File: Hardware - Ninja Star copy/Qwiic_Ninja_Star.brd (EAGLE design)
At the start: 87.6 x 41.9 mm, 29 parts, among them J1 QWIIC_RIGHT_ANGLE, J2 QWIIC_RIGHT_ANGLE, J3 QWIIC_RIGHT_ANGLE, J4 QWIIC_RIGHT_ANGLE

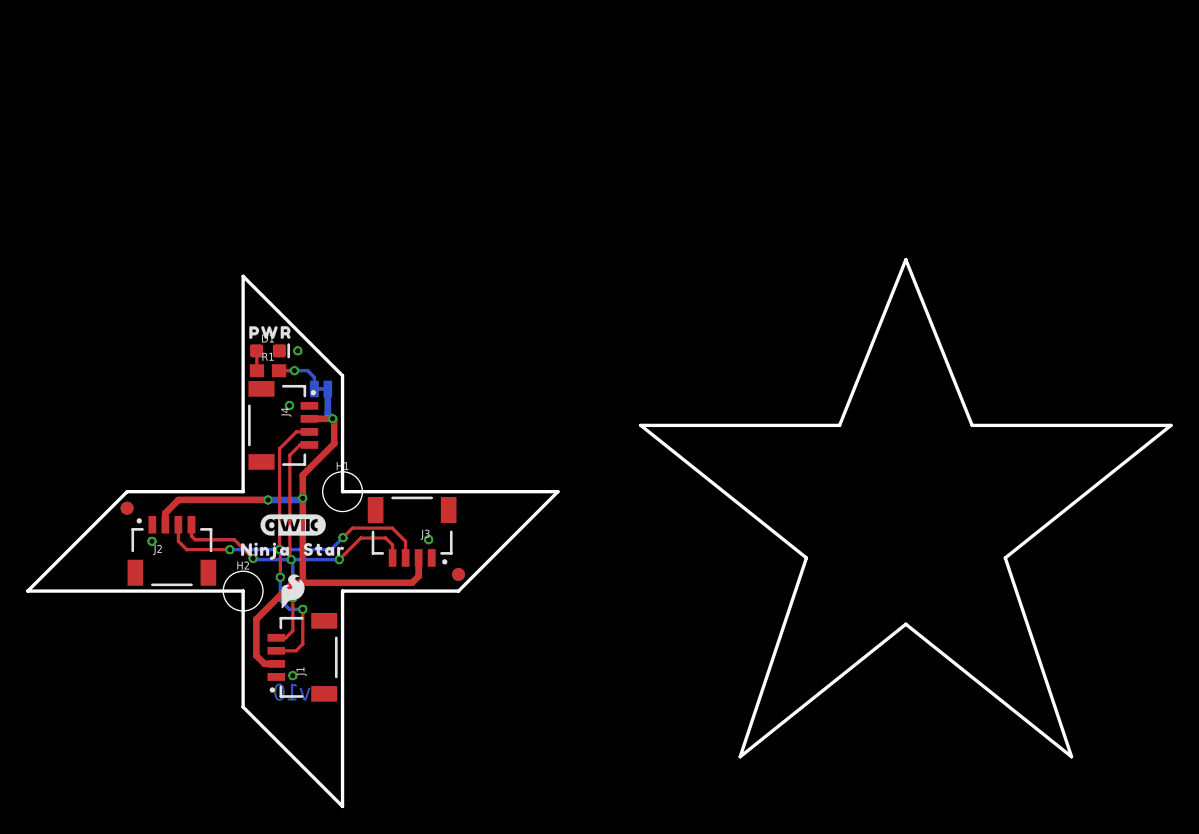
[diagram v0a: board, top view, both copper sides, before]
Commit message: Created star-shaped Qwiic Ninja Star and updated Multi Port
Updated Qwiic Multi Port with QC Double check concerns:
Removed wire stub
Approve DRC errors
Move via to not clip the t in "Port" on top
Moved power jumper and silk so that jumper silk and SF logo don't overlap
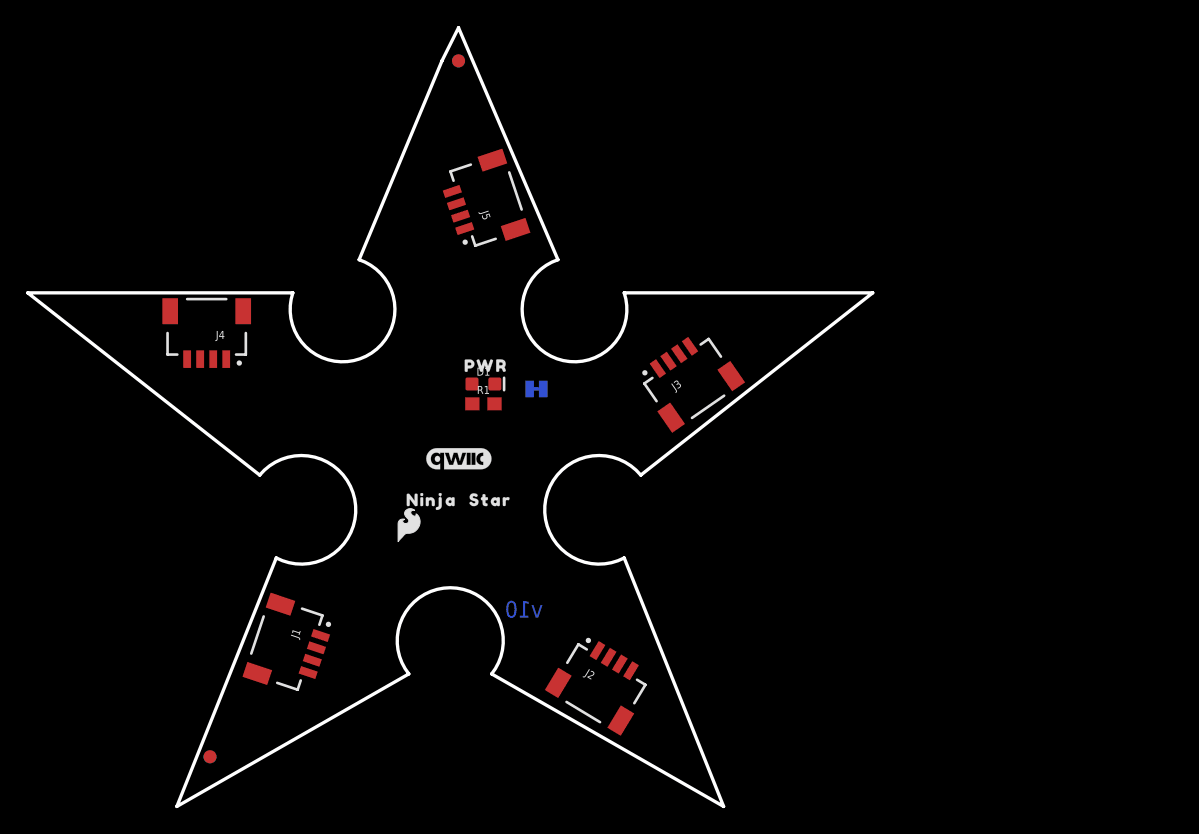
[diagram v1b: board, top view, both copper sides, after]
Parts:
- removed H1, H2: STAND-OFFTIGHT, SparkFun-Hardware:STAND-OFF-TIGHT
- added J5: QWIIC_RIGHT_ANGLE, SparkFun-Connectors:JST04_1MM_RA
- moved FD3 39.4 mm to (33.0, 57.1)
- moved FD4 39.4 mm to (33.0, 57.1)
- moved J2 35.5 mm to (45.0, 11.2), turned to 328.9 degrees
- moved J3 25.3 mm to (49.5, 34.4), turned to 34.7 degrees
- moved LOGO8 24.7 mm to (23.7, 32.1)
- moved LOGO7 21.3 mm to (29.0, 23.6)
- moved FD1 20.1 mm to (14.0, 3.81)
- moved FD2 20.1 mm to (14.0, 3.81)
- moved LOGO1 18.9 mm to (38.1, 20.3)
- moved LOGO3 18.9 mm to (33.0, 39.4)
- moved U$5 18.9 mm to (40.6, 18.5)
- moved U$7 18.9 mm to (40.3, 17.1)
- moved R1 16.7 mm to (34.9, 30.9)
- moved U$9 16.7 mm to (32.8, 33.8)
- moved D1 16.7 mm to (34.9, 32.4)
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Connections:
- net 3.3V: now also J5.2
- net GND: now also J5.1
- net SCL: now also J5.4
- net SDA: now also J5.3
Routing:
- net 3.3V: track 49.6 -> 0.00 mm, vias 3 -> 0
- net SDA: track 42.7 -> 0.00 mm, vias 5 -> 0
- net SCL: track 35.8 -> 0.00 mm, vias 4 -> 0
- net N$2: track 3.81 -> 0.02 mm, vias 1 -> 0
- net N$1: track 1.54 -> 0.00 mm
- removed copper zone on layer 1, net GND
- removed copper zone on layer 16, net GND
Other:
- board size 87.6 x 41.9 mm -> 64.8 x 59.7 mm

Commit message: Wired qwiic ninja star
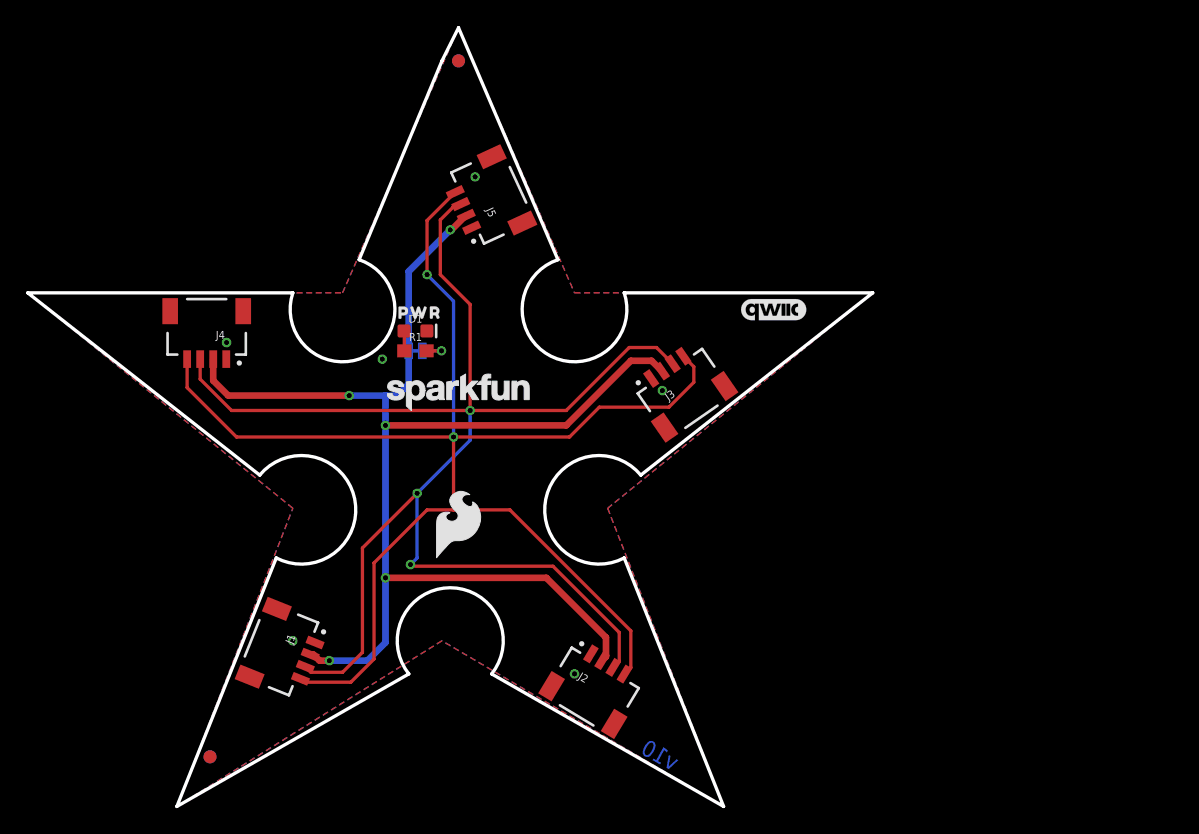
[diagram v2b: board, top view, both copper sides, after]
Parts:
- removed LOGO5, LOGO6, LOGO7, LOGO8: SFE_LOGO_FLAME.1_INCH, SparkFun-Aesthetics:SFE_LOGO_FLAME_.1
- removed U$3, U$5: (no value), output:NINJA0
- removed U$6, U$7: (no value), output:STAR0
- added U$1: (no value), SparkFun-Aesthetics:SFE_LOGO_NAME_.1
- U$2: device SparkFun-Aesthetics:SFE_LOGO_FLAME_.1 -> SparkFun-Aesthetics:SFE_LOGO_FLAME_.2
- moved LOGO2 26.7 mm to (57.1, 38.1)
- moved LOGO1 26.1 mm to (57.1, 38.1)
- moved LOGO3 19.0 mm to (33.0, 20.3)
- moved JP1 9.72 mm to (29.7, 34.9), turned to 0 degrees
- moved D1 6.61 mm to (29.7, 36.4)
- moved R1 6.61 mm to (29.7, 34.9)
- moved U$9 6.51 mm to (27.7, 37.8)
- moved U$4 5.97 mm to (35.2, 34.9)
- moved U$2 3.81 mm to (33.0, 21.6)
- moved J3 0.92 mm to (49.0, 33.7)
- moved J1 0.72 mm to (21.5, 11.2), turned to 248.1 degrees
- moved J2 0.57 mm to (44.5, 10.9)
- moved J5 0.38 mm to (33.4, 45.7), turned to 114.8 degrees
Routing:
- net SCL: track 0.00 -> 115.3 mm, vias 0 -> 2
- net SDA: track 0.00 -> 112.7 mm, vias 0 -> 3
- net 3.3V: track 0.00 -> 102.0 mm, vias 0 -> 5
- net N$2: track 0.02 -> 2.62 mm, vias 0 -> 1
- net N$1: track 0.00 -> 1.54 mm
- added copper zone on layer 1, net GND
- added copper zone on layer 16, net GND

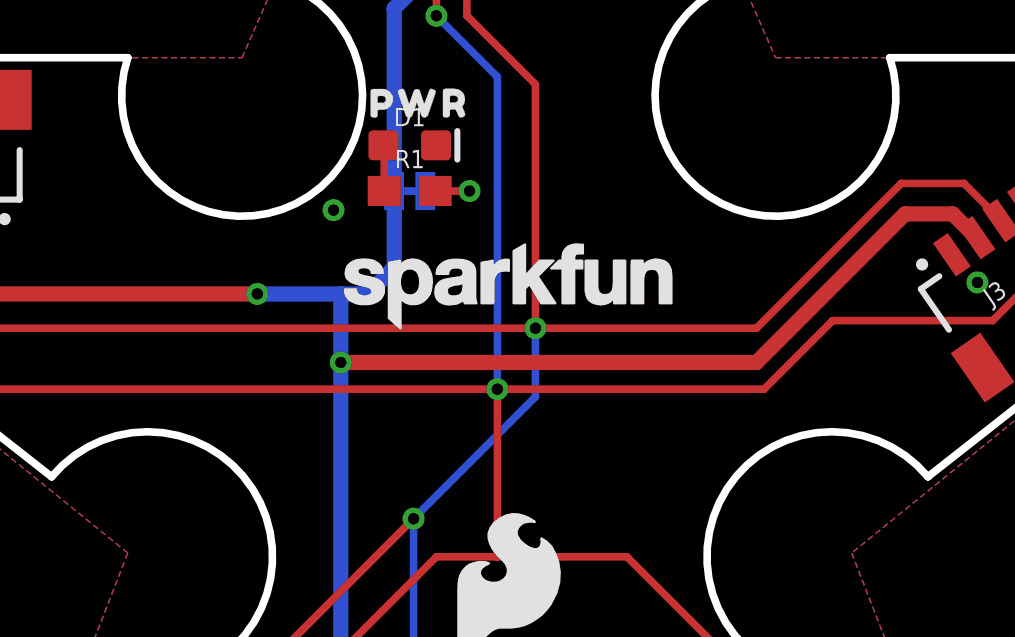
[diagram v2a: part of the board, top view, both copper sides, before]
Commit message: Update silk screen
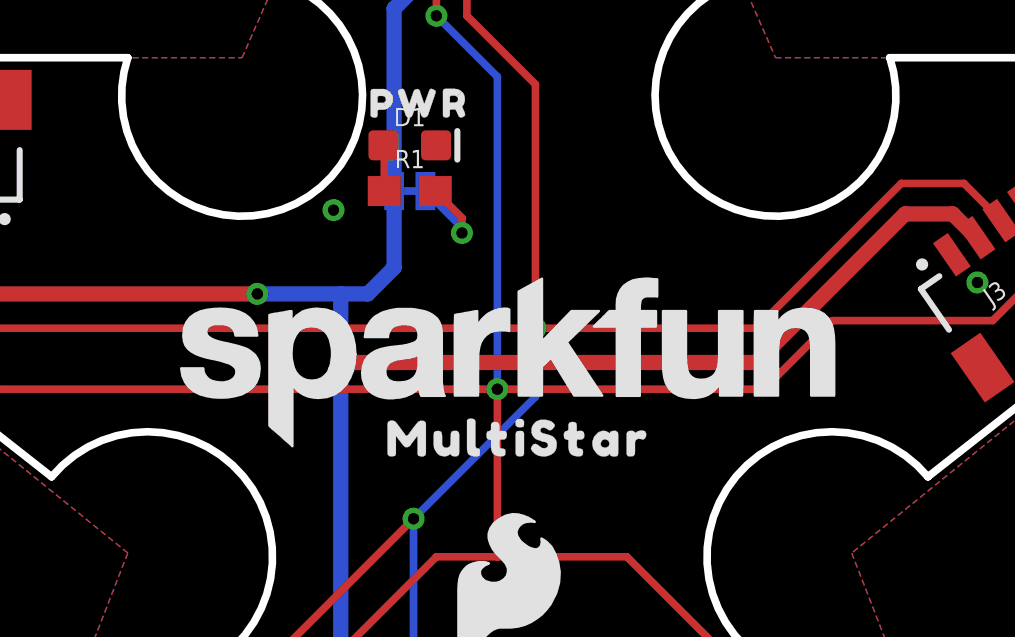
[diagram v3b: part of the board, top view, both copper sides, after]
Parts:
- removed U$1: (no value), SparkFun-Aesthetics:SFE_LOGO_NAME_.1
- removed U$4: (no value), output:PWR0
- added LOGO5: SFE_LOGO_NAME.2_INCH, SparkFun-Aesthetics:SFE_LOGO_NAME_.2
- added U$3, U$5: (no value), output:MULTISTAR0
- added U$6: (no value), output:#PWR#0
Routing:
- net N$2: track 2.62 -> 3.67 mm
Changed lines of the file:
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@@
 <?xml version="1.0" encoding="utf-8"?>
 <!DOCTYPE eagle SYSTEM "eagle.dtd">
-<eagle version="9.5.2">
+<eagle version="9.6.2">
 <drawing>
 <settings>
@@
 <element name="LOGO3" library="SparkFun-Aesthetics" package="OSHW-LOGO-S" value="OSHW-LOGOS" x="33.02" y="20.32" smashed="yes" rot="MR0"/>
 <element name="LOGO4" library="SparkFun-Aesthetics" package="SFE_LOGO_NAME_.2" value="SFE_LOGO_NAME.2_INCH" x="33.02" y="29.21" smashed="yes" rot="MR0"/>
-<element name="U$4" library="output" package="PWR0" value="" x="35.179" y="34.925" smashed="yes" rot="MR0"/>
 <element name="J5" library="SparkFun-Connectors" package="JST04_1MM_RA" value="QWIIC_RIGHT_ANGLE" x="33.401" y="45.72" smashed="yes" rot="R114.8">
 <attribute name="NAME" x="35.9468625" y="45.357428125" size="0.6096" layer="25" font="vector" ratio="20" rot="R114.8"/>
@@
 <attribute name="VALUE" x="37.09099375" y="45.6062875" size="0.6096" layer="27" font="vector" ratio="20" rot="R114.8"/>
 </element>
-<element name="U$1" library="SparkFun-Aesthetics" package="SFE_LOGO_NAME_.1" value="" x="33.02" y="31.75" smashed="yes"/>
 <element name="U$2" library="SparkFun-Aesthetics" package="SFE_LOGO_FLAME_.2" value="" x="33.02" y="21.59" smashed="yes"/>
+<element name="U$3" library="output" package="MULTISTAR0" value="" x="28.067" y="26.67" smashed="yes"/>
+<element name="U$5" library="output" package="MULTISTAR0" value="" x="38.481" y="26.67" smashed="yes" rot="MR0"/>
+<element name="U$6" library="output" package="#PWR#0" value="" x="35.306" y="34.925" smashed="yes" rot="MR0"/>
+<element name="LOGO5" library="SparkFun-Aesthetics" package="SFE_LOGO_NAME_.2" value="SFE_LOGO_NAME.2_INCH" x="33.02" y="29.21" smashed="yes"/>
 </elements>
 <signals>
@@
 <contactref element="JP1" pad="1"/>
 <contactref element="R1" pad="2"/>
-<wire x1="30.568" y1="34.925" x2="31.7119" y2="34.925" width="0.254" layer="1"/>
-<via x="31.7119" y="34.925" extent="1-16" drill="0.381"/>
-<wire x1="30.2387" y1="34.925" x2="31.7119" y2="34.925" width="0.254" layer="16"/>
+<wire x1="30.568" y1="34.925" x2="31.4579" y2="34.0351" width="0.254" layer="1"/>
+<wire x1="31.4579" y1="34.0351" x2="31.4579" y2="33.528" width="0.254" layer="1"/>
+<via x="31.4579" y="33.528" extent="1-16" drill="0.381"/>
+<wire x1="30.2387" y1="34.925" x2="31.4579" y2="33.7058" width="0.254" layer="16"/>
+<wire x1="31.4579" y1="33.7058" x2="31.4579" y2="33.528" width="0.254" layer="16"/>
 </signal>
 </signals>
